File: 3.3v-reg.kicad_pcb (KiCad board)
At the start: 2 copper layers, 6 parts, among them J1 USB_OTG, J2 Conn_01x02, J3 Conn_01x02, U1 AP1117-33

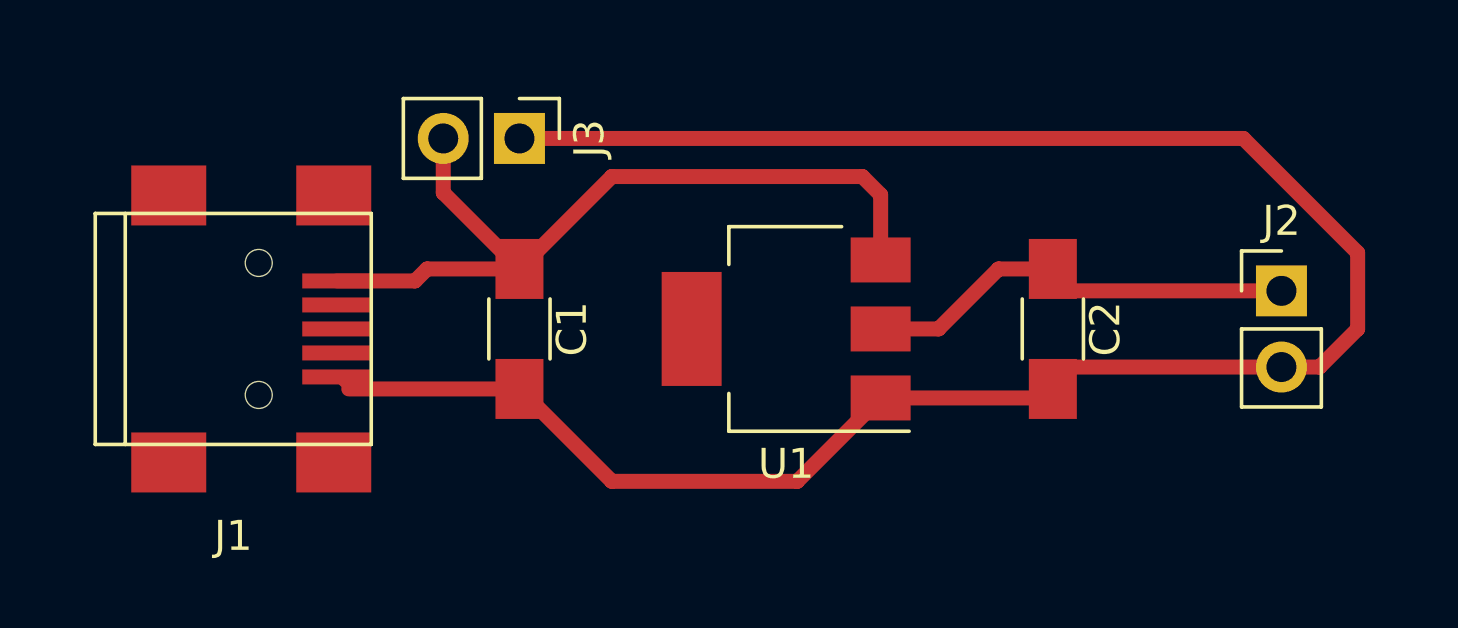
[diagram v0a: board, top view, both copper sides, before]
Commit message: Add Edge.Cuts layer
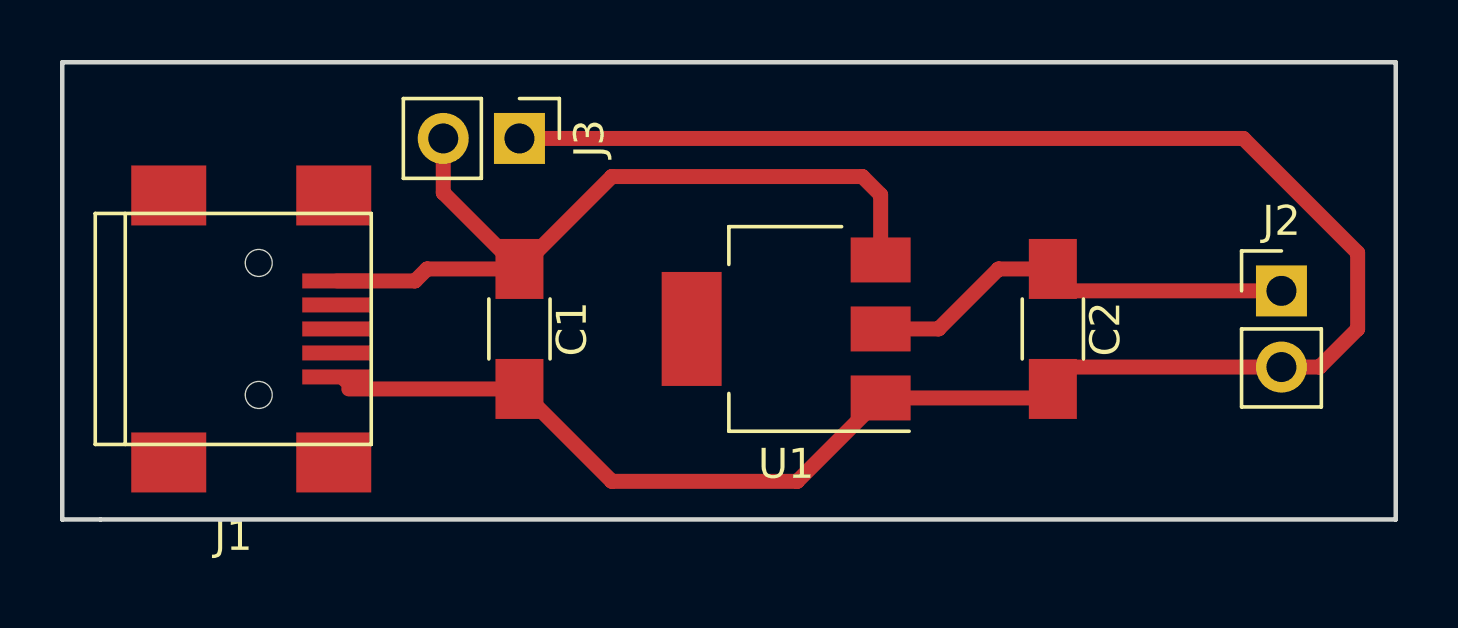
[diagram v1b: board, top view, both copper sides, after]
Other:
- board outline added: 44.5 x 15.2 mm
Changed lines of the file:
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@@
   (general
     (thickness 1.6)
-    (drawings 0)
+    (drawings 5)
     (tracks 27)
     (zones 0)
@@
     (42 Eco1.User user hide)
     (43 Eco2.User user hide)
-    (44 Edge.Cuts user hide)
+    (44 Edge.Cuts user)
     (45 Margin user hide)
     (46 B.CrtYd user hide)
@@
     )
   )
+  (gr_line (start 124.46 107.95) (end 125.73 107.95) (layer Edge.Cuts) (width 0.15))
+  (gr_line (start 124.46 92.71) (end 124.46 107.95) (layer Edge.Cuts) (width 0.15))
+  (gr_line (start 168.91 92.71) (end 124.46 92.71) (layer Edge.Cuts) (width 0.15))
+  (gr_line (start 168.91 107.95) (end 168.91 92.71) (layer Edge.Cuts) (width 0.15))
+  (gr_line (start 125.73 107.95) (end 168.91 107.95) (layer Edge.Cuts) (width 0.15))
   (segment (start 137.16 95.25) (end 137.16 97.06) (width 0.5) (layer F.Cu) (net 1))
   (segment (start 137.16 97.06) (end 139.7 99.6) (width 0.5) (layer F.Cu) (net 1))
